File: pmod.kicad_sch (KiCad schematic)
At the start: 7 parts, among them J4 Conn_2x6_P2.54mm_SAMTEC_SSW-1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, U14 TPD4E05U06QDQARQ1_ALT, U15 TPD4E05U06QDQARQ1_ALT

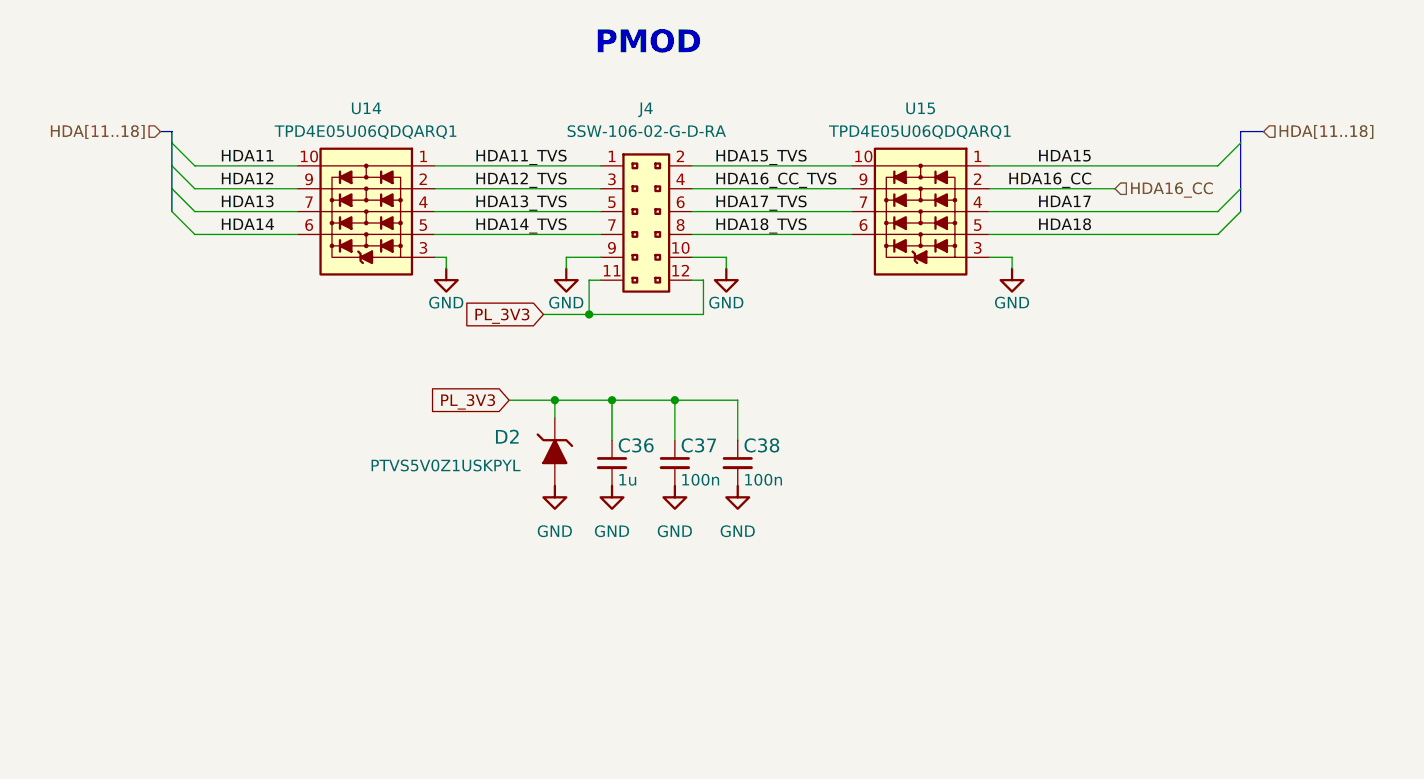
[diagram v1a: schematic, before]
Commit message: Replace studs, fix PMOD ESD diode pass, bump revision
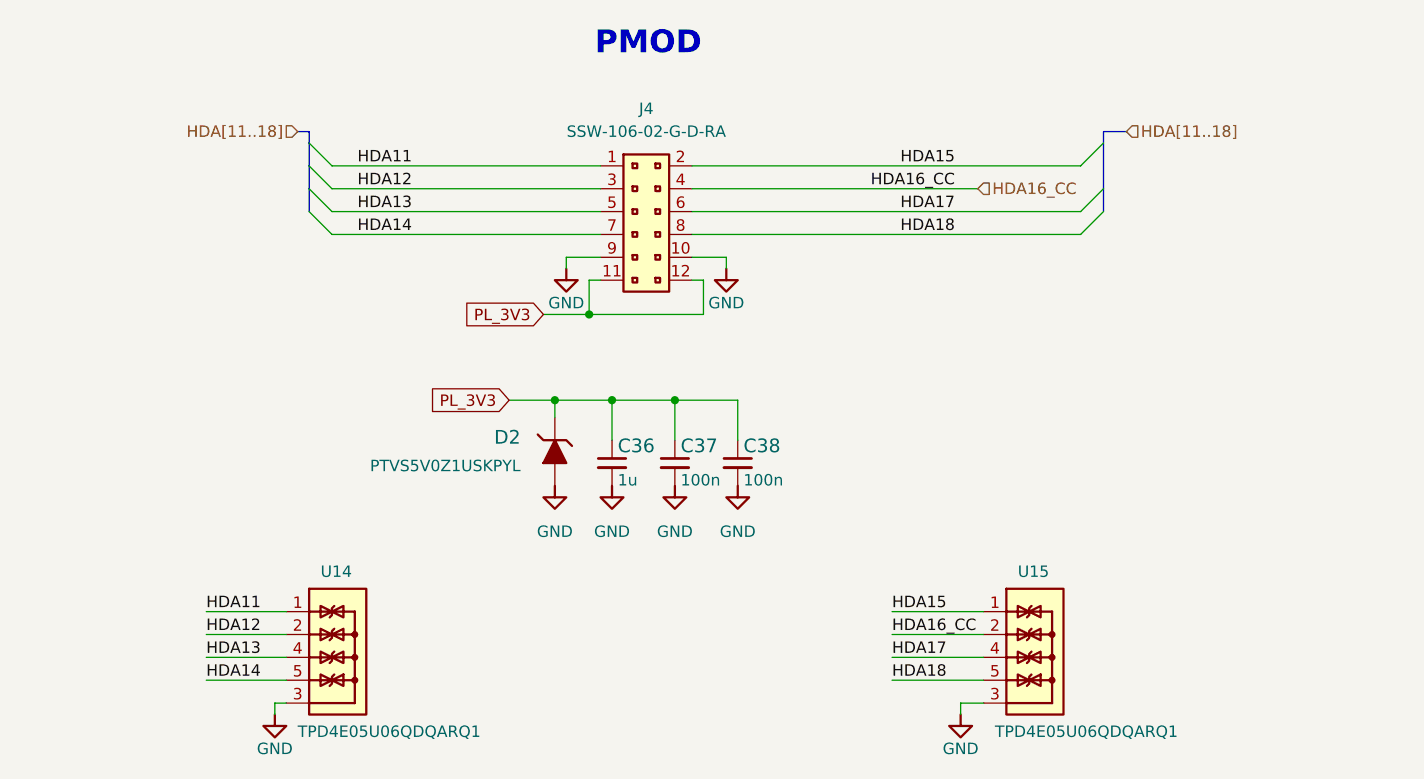
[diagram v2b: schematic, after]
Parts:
- removed U14, U15: TPD4E05U06QDQARQ1_ALT, kria-k26-devboard-footprints:USON-10_2.5x1mm_P0.5mm, symbol kria-k26-devboard:TPD4E05U06QDQARQ1_ALT
- added U14, U15: TPD4E05U06QDQARQ1, antmicro-footprints:USON-10_2.5x1mm_P0.5mm, symbol antmicroTVSDiodes:TPD4E05U06QDQARQ1
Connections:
- net HDA11_TVS is gone; now on net HDA11: J4.1
- net HDA12_TVS is gone; now on net HDA12: J4.3
- net HDA13_TVS is gone; now on net HDA13: J4.5
- net HDA14_TVS is gone; now on net HDA14: J4.7
- net HDA15_TVS is gone; now on net HDA15: J4.2
- net HDA16_CC_TVS is gone; now on net HDA16_CC: J4.4
- net HDA17_TVS is gone; now on net HDA17: J4.6
- net HDA18_TVS is gone; now on net HDA18: J4.8
- net GND: now also U14.3, U14.8, U15.3, U15.8
- net HDA11: now also U14.1, U14.10
- net HDA12: now also U14.2, U14.9
- net HDA13: now also U14.4, U14.7
- net HDA14: now also U14.5, U14.6
- net HDA15: now also U15.1, U15.10
- net HDA16_CC: now also U15.2, U15.9
- net HDA17: now also U15.4, U15.7
- net HDA18: now also U15.5, U15.6

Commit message: Loclib of the project
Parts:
- U14, U15: footprint antmicro-footprints:USON-10_2.5x1mm_P0.5mm -> kria-k26-devboard-footprints:USON-10_2.5x1mm_P0.5mm; symbol antmicroTVSDiodes:TPD4E05U06QDQARQ1 -> kria-k26-devboard:TPD4E05U06QDQARQ1

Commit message: [#56935] Update symbol/footprint links; Migrate to KiCad 7
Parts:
- C36: footprint kria-k26-devboard-footprints:C_0402_1005Metric -> antmicro-footprints:C_0402_1005Metric; symbol kria-k26-devboard:C_1u_0402 -> antmicroCapacitors0402:C_1u_0402
- C37, C38: footprint kria-k26-devboard-footprints:C_0402_1005Metric -> antmicro-footprints:C_0402_1005Metric; symbol kria-k26-devboard:C_100n_0402 -> antmicroCapacitors0402:C_100n_0402
- D2: footprint kria-k26-devboard-footprints:SOD-964 -> antmicro-footprints:SOD-964; symbol kria-k26-devboard:PTVS5V0Z1USKP -> antmicroTVSDiodes:PTVS5V0Z1USKP
- J4: footprint kria-k26-devboard-footprints:SAMTEC_SSW-106-02-G-D-RA -> antmicro-footprints:PinSocket_2x6_P2.54mm_Drill1.04mm_Horizontal; symbol kria-k26-devboard:Conn_2x6_P2.54mm_SAMTEC_SSW-106-02-G-D-RA -> antmicroGenericPinSockets:PinSocket_2x6_P2.54mm_Drill1.04mm_Horizontal
- U14, U15: footprint kria-k26-devboard-footprints:USON-10_2.5x1mm_P0.5mm -> antmicro-footprints:USON-10_2.5x1mm_P0.5mm; symbol kria-k26-devboard:TPD4E05U06QDQARQ1 -> antmicroTVSDiodes:TPD4E05U06QDQARQ1

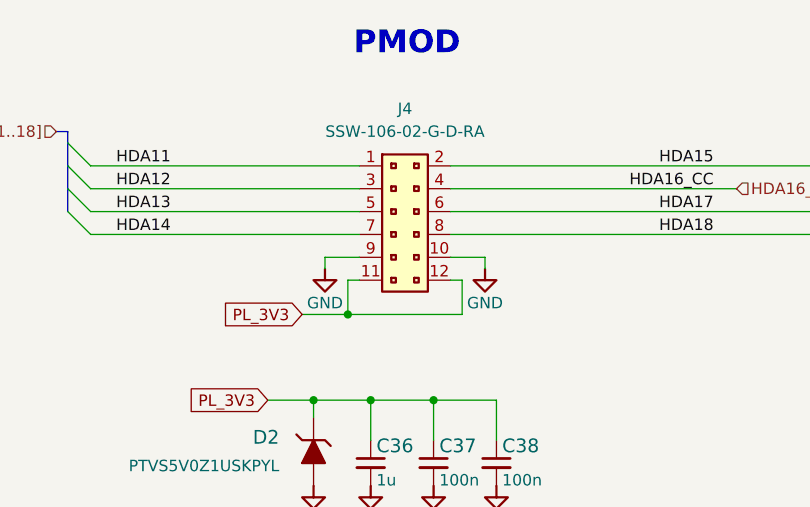
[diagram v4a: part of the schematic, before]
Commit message: [#56935] Fix missing highlights in OHP
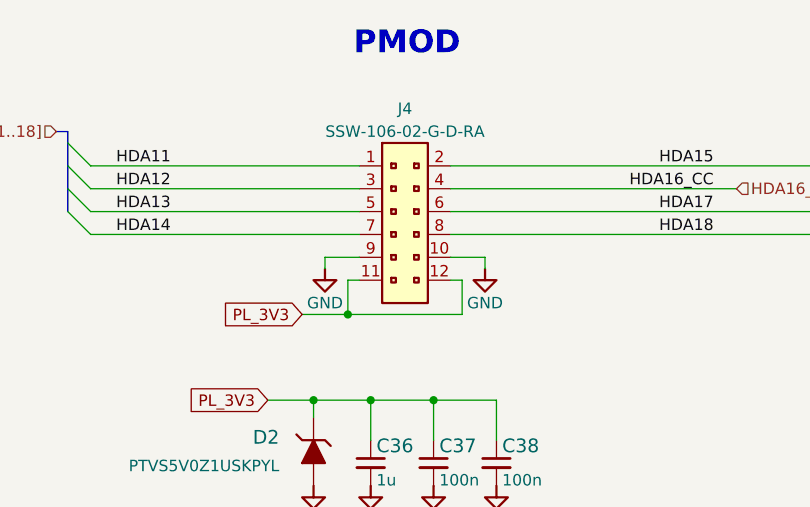
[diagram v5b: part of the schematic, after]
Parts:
- J4: value Conn_2x6_P2.54mm_SAMTEC_SSW-106-02-G-D-RA -> PinSocket_2x6_P2.54mm_Drill1.04mm_Horizontal
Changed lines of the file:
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@@
       (effects (font (size 1.27 1.27)))
     )
-    (property "Value" "Conn_2x6_P2.54mm_SAMTEC_SSW-106-02-G-D-RA" (at 210.185 134.62 0)
+    (property "Value" "PinSocket_2x6_P2.54mm_Drill1.04mm_Horizontal" (at 210.185 134.62 0)
       (effects (font (size 1.27 1.27) (thickness 0.15)) hide)
     )

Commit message: [#56935] Loclib
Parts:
- C36: footprint antmicro-footprints:C_0402_1005Metric -> kria-k26-devboard-footprints:C_0402_1005Metric; symbol antmicroCapacitors0402:C_1u_0402 -> kria-k26-devboard:C_1u_0402
- C37, C38: footprint antmicro-footprints:C_0402_1005Metric -> kria-k26-devboard-footprints:C_0402_1005Metric; symbol antmicroCapacitors0402:C_100n_0402 -> kria-k26-devboard:C_100n_0402
- D2: footprint antmicro-footprints:SOD-964 -> kria-k26-devboard-footprints:SOD-964; symbol antmicroTVSDiodes:PTVS5V0Z1USKP -> kria-k26-devboard:PTVS5V0Z1USKP
- J4: footprint antmicro-footprints:PinSocket_2x6_P2.54mm_Drill1.04mm_Horizontal -> kria-k26-devboard-footprints:PinSocket_2x6_P2.54mm_Drill1.04mm_Horizontal; symbol antmicroGenericPinSockets:PinSocket_2x6_P2.54mm_Drill1.04mm_Horizontal -> kria-k26-devboard:PinSocket_2x6_P2.54mm_Drill1.04mm_Horizontal
- U14, U15: footprint antmicro-footprints:USON-10_2.5x1mm_P0.5mm -> kria-k26-devboard-footprints:USON-10_2.5x1mm_P0.5mm; symbol antmicroTVSDiodes:TPD4E05U06QDQARQ1 -> kria-k26-devboard:TPD4E05U06QDQARQ1
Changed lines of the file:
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@@
     (effects (font (size 1.27 1.27)) (justify left))
   )
-  (symbol (lib_id "antmicroGenericPinSockets:PinSocket_2x6_P2.54mm_Drill1.04mm_Horizontal") (at 205.105 138.43 0) (unit 1)
+  (symbol (lib_id "kria-k26-devboard:PinSocket_2x6_P2.54mm_Drill1.04mm_Horizontal") (at 205.105 138.43 0) (unit 1)
     (in_bom yes) (on_board yes) (dnp no) (fields_autoplaced)
     (property "Reference" "J4" (at 210.185 132.08 0)
@@
       (effects (font (size 1.27 1.27) (thickness 0.15)) hide)
     )
-    (property "Footprint" "antmicro-footprints:PinSocket_2x6_P2.54mm_Drill1.04mm_Horizontal" (at 224.155 143.51 0)
+    (property "Footprint" "kria-k26-devboard-footprints:PinSocket_2x6_P2.54mm_Drill1.04mm_Horizontal" (at 224.155 143.51 0)
       (effects (font (size 1.27 1.27) (thickness 0.15)) (justify left bottom) hide)
     )
@@
     )
   )
-  (symbol (lib_id "antmicropower:GND") (at 201.295 149.86 0) (unit 1)
+  (symbol (lib_id "kria-k26-devboard:GND") (at 201.295 149.86 0) (unit 1)
     (in_bom yes) (on_board yes) (dnp no)
     (property "Reference" "#PWR065" (at 201.295 156.21 0)
@@
     )
   )
-  (symbol (lib_id "antmicropower:GND") (at 219.075 149.86 0) (unit 1)
+  (symbol (lib_id "kria-k26-devboard:GND") (at 219.075 149.86 0) (unit 1)
     (in_bom yes) (on_board yes) (dnp no)
     (property "Reference" "#PWR067" (at 219.075 156.21 0)
@@
     )
   )
-  (symbol (lib_id "antmicroCapacitors0402:C_100n_0402") (at 213.36 168.91 270) (unit 1)
+  (symbol (lib_id "kria-k26-devboard:C_100n_0402") (at 213.36 168.91 270) (unit 1)
     (in_bom yes) (on_board yes) (dnp no)
     (property "Reference" "C37" (at 213.995 169.545 90)
@@
       (effects (font (size 1.27 1.27) (thickness 0.15)) (justify left bottom) hide)
     )
-    (property "Footprint" "antmicro-footprints:C_0402_1005Metric" (at 200.66 189.23 0)
+    (property "Footprint" "kria-k26-devboard-footprints:C_0402_1005Metric" (at 200.66 189.23 0)
       (effects (font (size 1.27 1.27) (thickness 0.15)) (justify left bottom) hide)
     )
@@
     )
   )
-  (symbol (lib_id "antmicroCapacitors0402:C_100n_0402") (at 220.345 168.91 270) (unit 1)
+  (symbol (lib_id "kria-k26-devboard:C_100n_0402") (at 220.345 168.91 270) (unit 1)
     (in_bom yes) (on_board yes) (dnp no)
     (property "Reference" "C38" (at 220.98 169.545 90)
@@
       (effects (font (size 1.27 1.27) (thickness 0.15)) (justify left bottom) hide)
     )
-    (property "Footprint" "antmicro-footprints:C_0402_1005Metric" (at 207.645 189.23 0)
+    (property "Footprint" "kria-k26-devboard-footprints:C_0402_1005Metric" (at 207.645 189.23 0)
       (effects (font (size 1.27 1.27) (thickness 0.15)) (justify left bottom) hide)
     )
@@
     )
   )
-  (symbol (lib_id "antmicroCapacitors0402:C_1u_0402") (at 206.375 168.91 270) (unit 1)
+  (symbol (lib_id "kria-k26-devboard:C_1u_0402") (at 206.375 168.91 270) (unit 1)
     (in_bom yes) (on_board yes) (dnp no)
     (property "Reference" "C36" (at 207.01 169.545 90)
@@
       (effects (font (size 1.27 1.27) (thickness 0.15)) (justify left bottom) hide)
     )
-    (property "Footprint" "antmicro-footprints:C_0402_1005Metric" (at 193.675 189.23 0)
+    (property "Footprint" "kria-k26-devboard-footprints:C_0402_1005Metric" (at 193.675 189.23 0)
       (effects (font (size 1.27 1.27) (thickness 0.15)) (justify left bottom) hide)
     )
@@
     )
   )
-  (symbol (lib_id "antmicropower:GND") (at 220.345 173.99 0) (unit 1)
+  (symbol (lib_id "kria-k26-devboard:GND") (at 220.345 173.99 0) (unit 1)
     (in_bom yes) (on_board yes) (dnp no) (fields_autoplaced)
     (property "Reference" "#PWR066" (at 220.345 180.34 0)
@@
     )
   )
-  (symbol (lib_id "antmicropower:GND") (at 168.91 199.39 0) (unit 1)
+  (symbol (lib_id "kria-k26-devboard:GND") (at 168.91 199.39 0) (unit 1)
     (in_bom yes) (on_board yes) (dnp no)
     (property "Reference" "#PWR064" (at 168.91 205.74 0)
@@
     )
   )
-  (symbol (lib_id "antmicropower:GND") (at 245.11 199.39 0) (mirror y) (unit 1)
+  (symbol (lib_id "kria-k26-devboard:GND") (at 245.11 199.39 0) (mirror y) (unit 1)
     (in_bom yes) (on_board yes) (dnp no)
     (property "Reference" "#PWR068" (at 245.11 205.74 0)
@@
     )
   )
-  (symbol (lib_id "antmicroTVSDiodes:PTVS5V0Z1USKP") (at 200.025 173.99 90) (unit 1)
+  (symbol (lib_id "kria-k26-devboard:PTVS5V0Z1USKP") (at 200.025 173.99 90) (unit 1)
     (in_bom yes) (on_board yes) (dnp no) (fields_autoplaced)
     (property "Reference" "D2" (at 196.215 168.5925 90)
@@
       (effects (font (size 1.27 1.27) (thickness 0.15)) (justify left bottom) hide)
     )
-    (property "Footprint" "antmicro-footprints:SOD-964" (at 207.645 152.4 0)
+    (property "Footprint" "kria-k26-devboard-footprints:SOD-964" (at 207.645 152.4 0)
       (effects (font (size 1.27 1.27) (thickness 0.15)) (justify left bottom) hide)
     )
@@
     )
   )
-  (symbol (lib_id "antmicroTVSDiodes:TPD4E05U06QDQARQ1") (at 247.65 187.96 0) (unit 1)
+  (symbol (lib_id "kria-k26-devboard:TPD4E05U06QDQARQ1") (at 247.65 187.96 0) (unit 1)
     (in_bom yes) (on_board yes) (dnp no)
     (property "Reference" "U15" (at 251.46 183.515 0)
@@
       (effects (font (size 1.27 1.27) (thickness 0.15)) (justify left))
     )
-    (property "Footprint" "antmicro-footprints:USON-10_2.5x1mm_P0.5mm" (at 271.78 193.04 0)
+    (property "Footprint" "kria-k26-devboard-footprints:USON-10_2.5x1mm_P0.5mm" (at 271.78 193.04 0)
       (effects (font (size 1.27 1.27) (thickness 0.15)) (justify left bottom) hide)
     )
@@
     )
   )
-  (symbol (lib_id "antmicropower:GND") (at 206.375 173.99 0) (unit 1)
+  (symbol (lib_id "kria-k26-devboard:GND") (at 206.375 173.99 0) (unit 1)
     (in_bom yes) (on_board yes) (dnp no) (fields_autoplaced)
     (property "Reference" "#PWR0368" (at 206.375 180.34 0)
@@
     )
   )
-  (symbol (lib_id "antmicroTVSDiodes:TPD4E05U06QDQARQ1") (at 170.18 187.96 0) (unit 1)
+  (symbol (lib_id "kria-k26-devboard:TPD4E05U06QDQARQ1") (at 170.18 187.96 0) (unit 1)
     (in_bom yes) (on_board yes) (dnp no)
     (property "Reference" "U14" (at 173.99 183.515 0)
@@
       (effects (font (size 1.27 1.27) (thickness 0.15)) (justify left))
     )
-    (property "Footprint" "antmicro-footprints:USON-10_2.5x1mm_P0.5mm" (at 194.31 193.04 0)
+    (property "Footprint" "kria-k26-devboard-footprints:USON-10_2.5x1mm_P0.5mm" (at 194.31 193.04 0)
       (effects (font (size 1.27 1.27) (thickness 0.15)) (justify left bottom) hide)
     )
@@
     )
   )
-  (symbol (lib_id "antmicropower:GND") (at 200.025 173.99 0) (unit 1)
+  (symbol (lib_id "kria-k26-devboard:GND") (at 200.025 173.99 0) (unit 1)
     (in_bom yes) (on_board yes) (dnp no) (fields_autoplaced)
     (property "Reference" "#PWR0378" (at 200.025 180.34 0)
@@
     )
   )
-  (symbol (lib_id "antmicropower:GND") (at 213.36 173.99 0) (unit 1)
+  (symbol (lib_id "kria-k26-devboard:GND") (at 213.36 173.99 0) (unit 1)
     (in_bom yes) (on_board yes) (dnp no) (fields_autoplaced)
     (property "Reference" "#PWR0371" (at 213.36 180.34 0)
